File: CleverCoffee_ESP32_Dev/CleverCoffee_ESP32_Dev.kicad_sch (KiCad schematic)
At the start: 25 parts

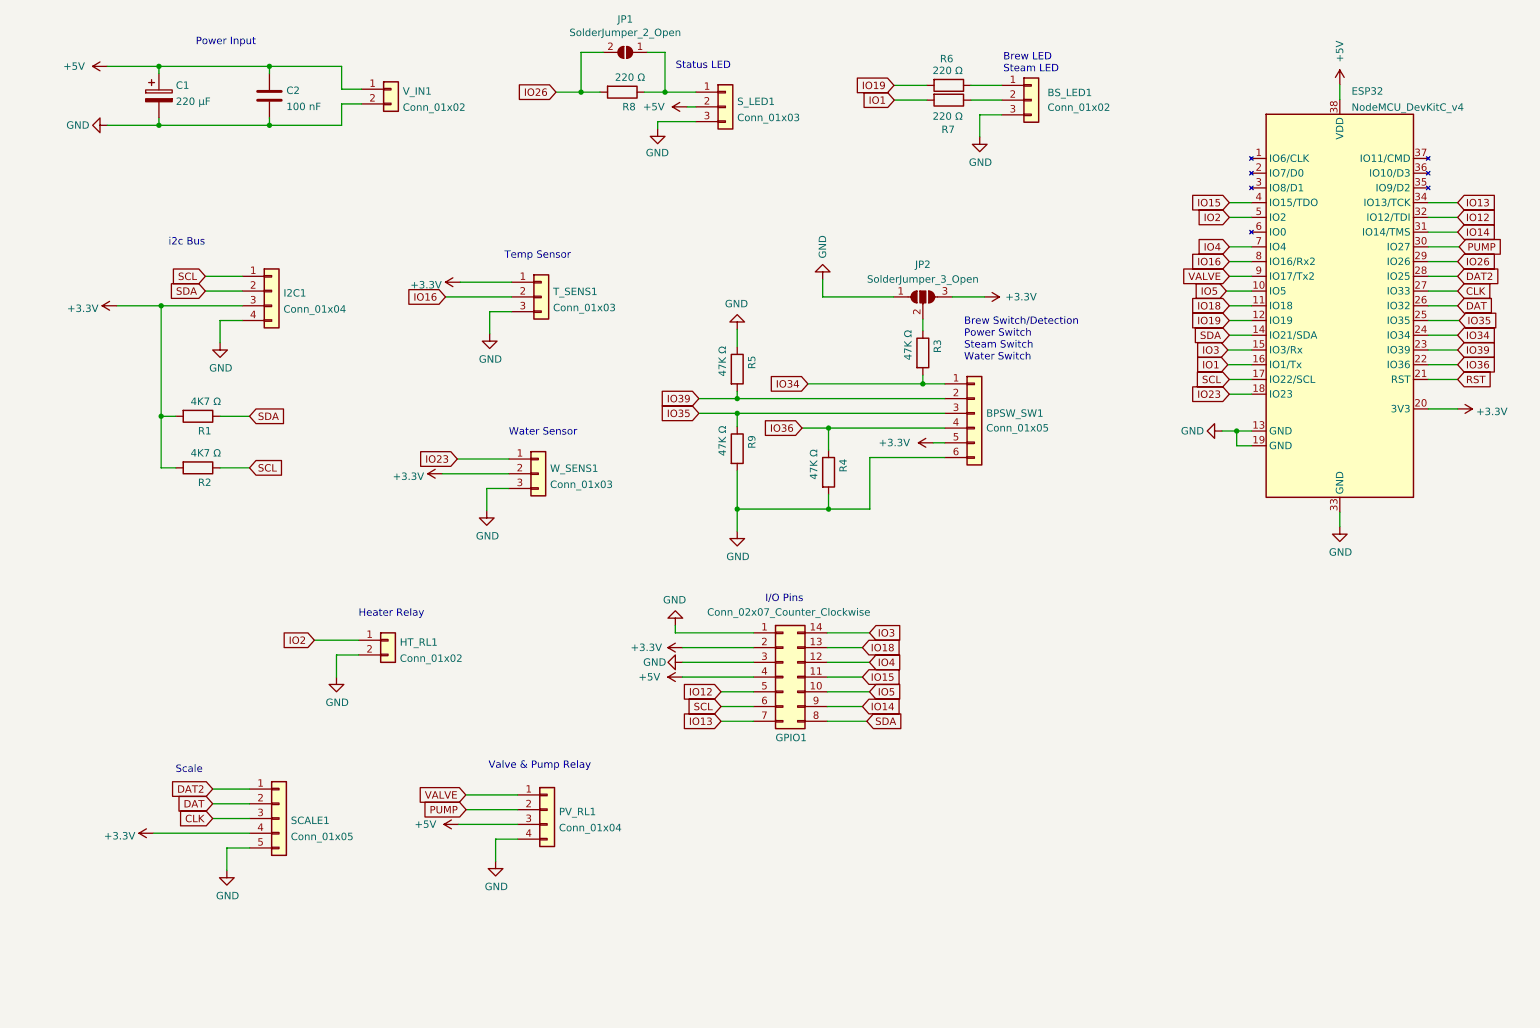
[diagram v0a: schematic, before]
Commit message: Add new SMD variant of the Dev PCB, make naming scheme consistent
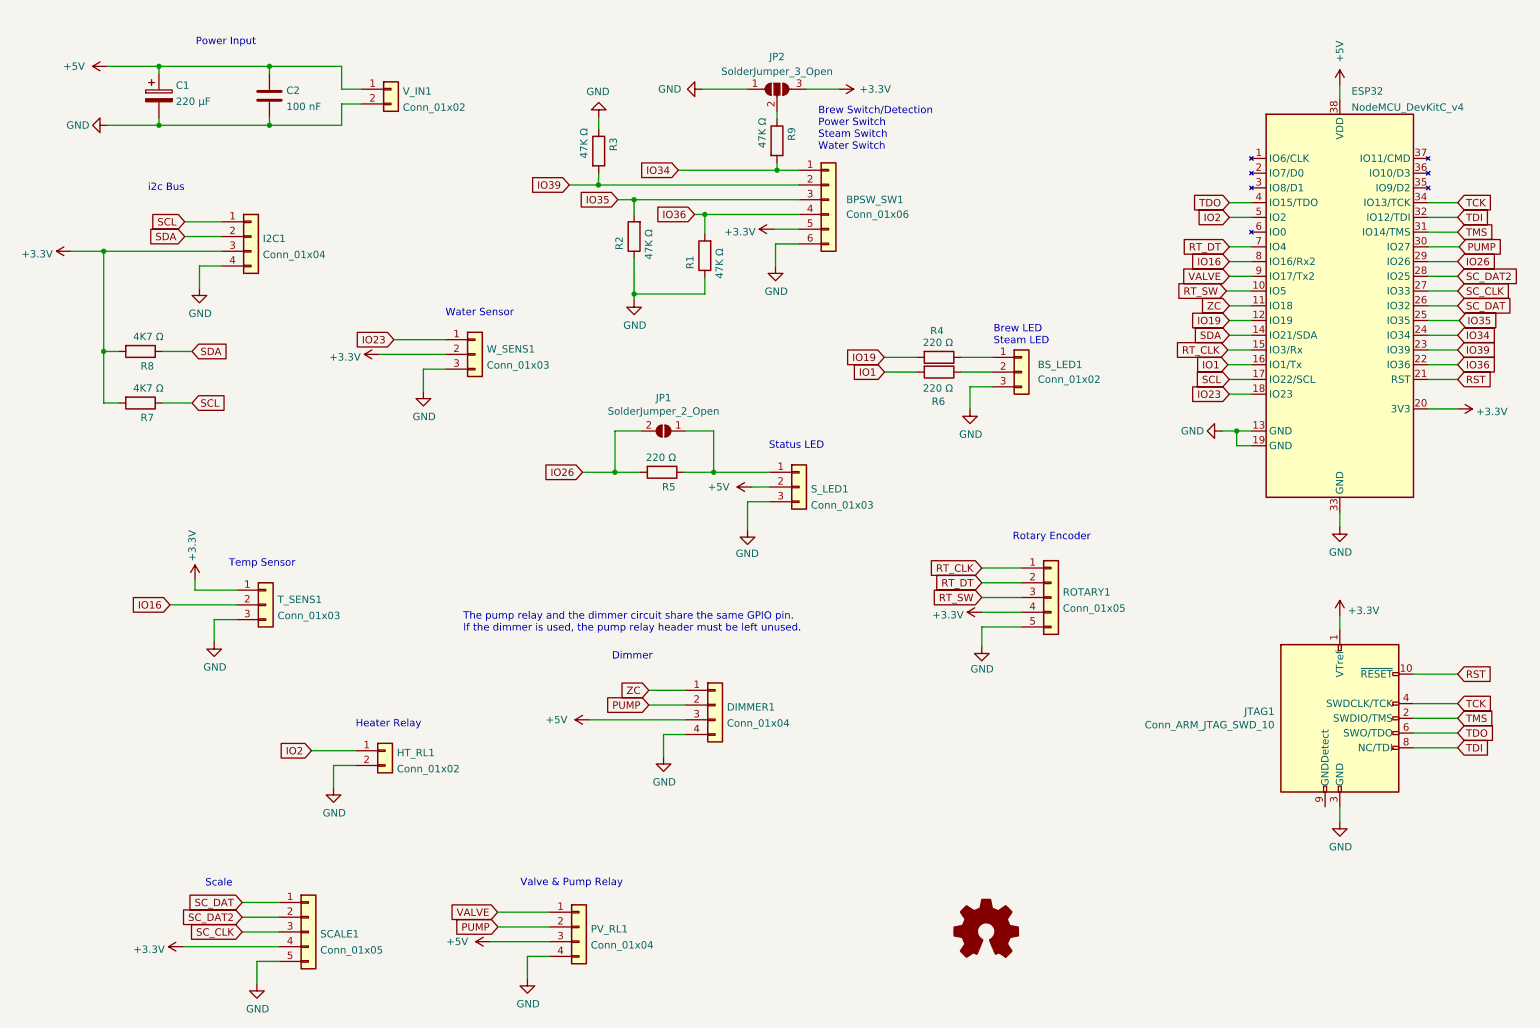
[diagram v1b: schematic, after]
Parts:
- removed GPIO1: Conn_02x07_Counter_Clockwise, Connector_PinSocket_2.54mm:PinSocket_2x07_P2.54mm_Vertical, symbol Connector_Generic:Conn_02x07_Counter_Clockwise
- removed R7: 220 Ω, Resistor_SMD:R_1206_3216Metric_Pad1.30x1.75mm_HandSolder, symbol Device:R
- added DIMMER1: Conn_01x04, Connector_PinSocket_2.54mm:PinSocket_1x04_P2.54mm_Vertical, symbol Connector_Generic:Conn_01x04
- added JTAG1: Conn_ARM_JTAG_SWD_10, Connector_PinHeader_2.54mm:PinHeader_2x05_P2.54mm_Vertical, symbol Connector:Conn_ARM_JTAG_SWD_10
- added R1: 47K Ω, Resistor_THT:R_Axial_DIN0207_L6.3mm_D2.5mm_P10.16mm_Horizontal, symbol Device:R
- added ROTARY1: Conn_01x05, Connector_PinSocket_2.54mm:PinSocket_1x05_P2.54mm_Vertical, symbol Connector_Generic:Conn_01x05
- BPSW_SW1: value Conn_01x05 -> Conn_01x06
- C1: footprint Capacitor_SMD:CP_Elec_6.3x7.7 -> Capacitor_THT:CP_Radial_D8.0mm_P3.80mm
- C2: footprint Capacitor_SMD:C_1206_3216Metric_Pad1.33x1.80mm_HandSolder -> Capacitor_THT:C_Axial_L5.1mm_D3.1mm_P7.50mm_Horizontal
- R2: renamed from R9; footprint Resistor_SMD:R_1206_3216Metric_Pad1.30x1.75mm_HandSolder -> Resistor_THT:R_Axial_DIN0207_L6.3mm_D2.5mm_P10.16mm_Horizontal
- R3: renamed from R5; footprint Resistor_SMD:R_1206_3216Metric_Pad1.30x1.75mm_HandSolder -> Resistor_THT:R_Axial_DIN0207_L6.3mm_D2.5mm_P10.16mm_Horizontal
- R4: value 47K Ω -> 220 Ω; footprint Resistor_SMD:R_1206_3216Metric_Pad1.30x1.75mm_HandSolder -> Resistor_THT:R_Axial_DIN0207_L6.3mm_D2.5mm_P10.16mm_Horizontal
- R5: renamed from R8; footprint Resistor_SMD:R_1206_3216Metric_Pad1.30x1.75mm_HandSolder -> Resistor_THT:R_Axial_DIN0207_L6.3mm_D2.5mm_P10.16mm_Horizontal
- R6: footprint Resistor_SMD:R_1206_3216Metric_Pad1.30x1.75mm_HandSolder -> Resistor_THT:R_Axial_DIN0207_L6.3mm_D2.5mm_P10.16mm_Horizontal
- R7: renamed from R2; footprint Resistor_SMD:R_1206_3216Metric_Pad1.30x1.75mm_HandSolder -> Resistor_THT:R_Axial_DIN0207_L6.3mm_D2.5mm_P10.16mm_Horizontal
- R8: renamed from R1; footprint Resistor_SMD:R_1206_3216Metric_Pad1.30x1.75mm_HandSolder -> Resistor_THT:R_Axial_DIN0207_L6.3mm_D2.5mm_P10.16mm_Horizontal
- R9: renamed from R3; footprint Resistor_SMD:R_1206_3216Metric_Pad1.30x1.75mm_HandSolder -> Resistor_THT:R_Axial_DIN0207_L6.3mm_D2.5mm_P10.16mm_Horizontal
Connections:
- net +3V3: now also JTAG1.1 (VTref), ROTARY1.4 (Pin_4)
- net +5V: now also DIMMER1.3 (Pin_3)
- net GND: now also R2.1, DIMMER1.4 (Pin_4), JTAG1.3 (GND), JTAG1.5 (GND), R1.1, ROTARY1.5 (Pin_5); no longer R2.2, R4.2
- net IO1: now also R6.2
- net IO19: now also R4.2; no longer R6.2
- net IO35: now also R2.2; no longer R2.1
- net IO36: now also R1.2; no longer R4.1
- net PUMP: now also DIMMER1.2 (Pin_2)
- net RST: now also JTAG1.10 (~{RESET})
- net at BS_LED1.2 (Pin_2): now also R6.1
- net at BS_LED1.1 (Pin_1): now also R4.1; no longer R6.1
- net CLK renamed SC_CLK
- net DAT renamed SC_DAT
- net SC_DAT: now also SCALE1.1 (Pin_1); no longer SCALE1.2 (Pin_2)
- net DAT2 renamed SC_DAT2
- net SC_DAT2: now also SCALE1.2 (Pin_2); no longer SCALE1.1 (Pin_1)
- net IO12 renamed TDI
- net TDI: now also JTAG1.8 (NC/TDI)
- net IO13 renamed TCK
- net TCK: now also JTAG1.4 (SWDCLK/TCK)
- net IO14 renamed TMS
- net TMS: now also JTAG1.2 (SWDIO/TMS)
- net IO15 renamed TDO
- net TDO: now also JTAG1.6 (SWO/TDO)
- net IO18 renamed ZC
- net ZC: now also DIMMER1.1 (Pin_1)
- net IO3 renamed RT_CLK
- net RT_CLK: now also ROTARY1.1 (Pin_1)
- net IO4 renamed RT_DT
- net RT_DT: now also ROTARY1.2 (Pin_2)
- net IO5 renamed RT_SW
- net RT_SW: now also ROTARY1.3 (Pin_3)
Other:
- note added: "Dimmer"
- note added: "Rotary Encoder"
- note added: "The pump relay and the dimmer circuit share the same GPIO pin. If the dimmer is used, the pump relay header must be left unused."
- note removed: "I/O Pins"
- title: ESP32 Breakout Board - SMD -> ESP32 Breakout Board
- moved on the sheet: HT_RL1, I2C1, JP1, PV_RL1, R2, R3, R5, R7, R8, R9, SCALE1, S_LED1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
